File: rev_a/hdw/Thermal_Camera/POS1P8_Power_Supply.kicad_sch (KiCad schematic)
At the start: 21 parts

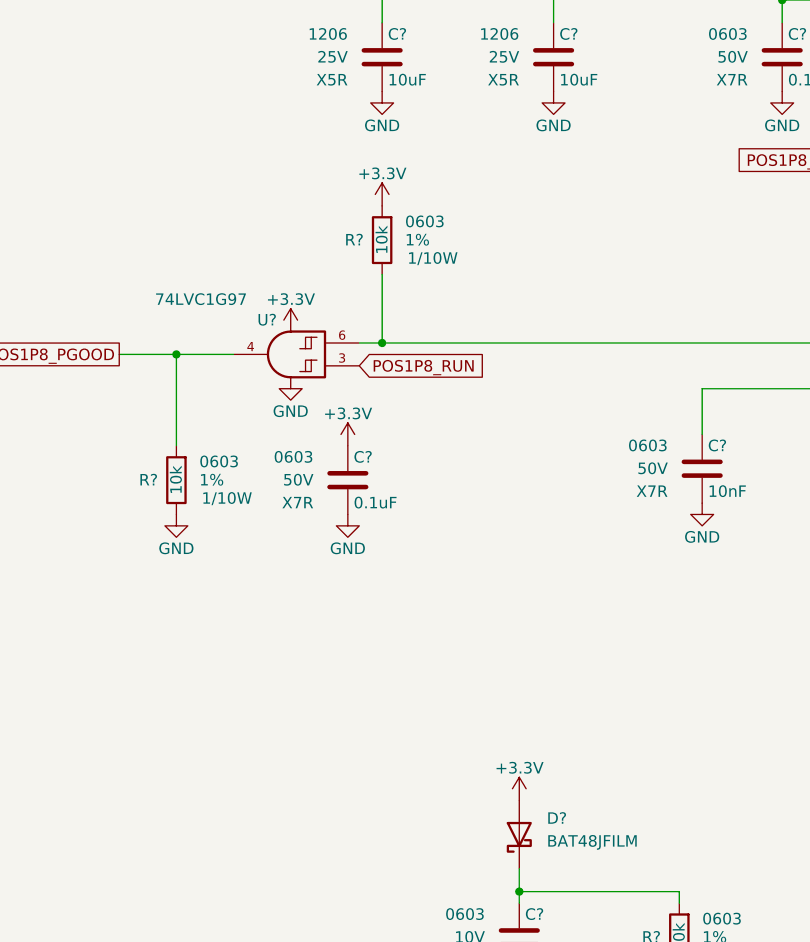
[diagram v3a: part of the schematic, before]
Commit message: changed a lot of circuits from +3.3V to +3.0V VDD
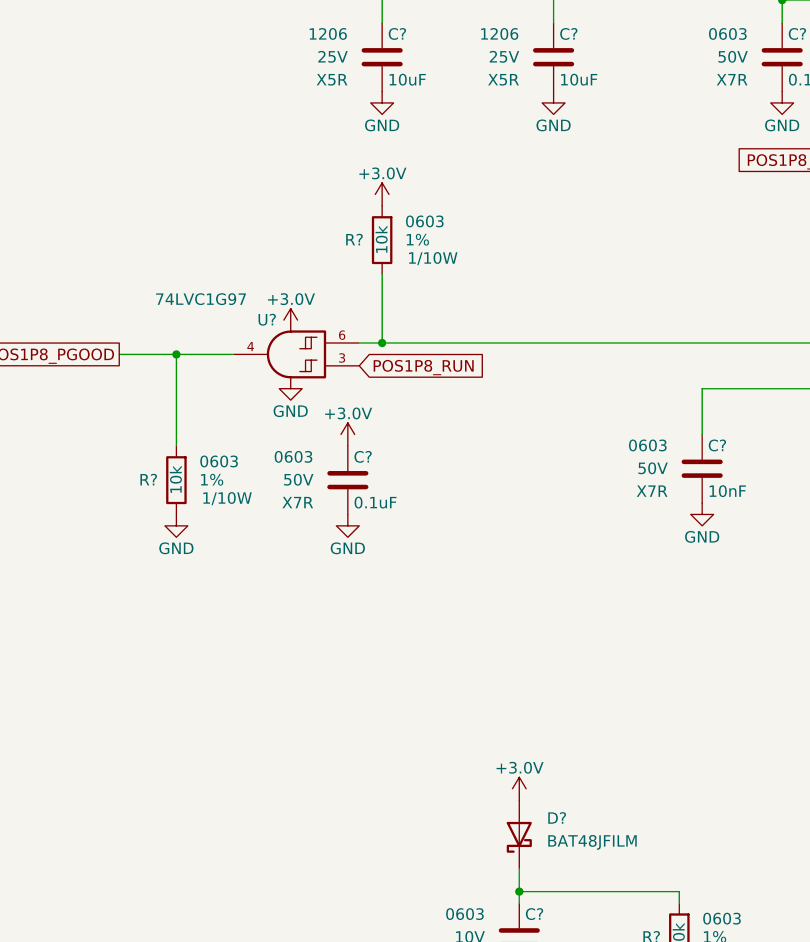
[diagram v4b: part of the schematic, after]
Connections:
- net +3.3V renamed +3.0V
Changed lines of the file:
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@@
-    )
-  )
-  (symbol (lib_id "power:+3.3V") (at 88.9 140.97 0) (unit 1)
-    (in_bom yes) (on_board yes) (dnp no)
-    (property "Reference" "#PWR0609" (at 88.9 144.78 0)
-      (effects (font (size 1.27 1.27)) hide)
-    )
-    (property "Value" "+3.3V" (at 88.9 137.414 0)
-      (effects (font (size 1.27 1.27)))
-    )
-    (property "Footprint" "" (at 88.9 140.97 0)
-      (effects (font (size 1.27 1.27)) hide)
-    )
-    (property "Datasheet" "" (at 88.9 140.97 0)
-      (effects (font (size 1.27 1.27)) hide)
-    )
-    (pin "1")
-    (instances
-      (project "Thermal_Camera"
-        (path "/4bd21e0b-5408-4b93-866e-c82ac5b31fa9/3fa2ed45-8dc3-4842-ae64-2bab78bff715"
-          (reference "#PWR0609") (unit 1)
-        )
-      )
     )
   )
@@
         (path "/e85aac8c-404c-45dd-bda3-1057cae83baf/00000000-0000-0000-0000-00005f41a7c7"
           (reference "#PWR0322") (unit 1)
-        )
-      )
-    )
-  )
-  (symbol (lib_id "power:+3.3V") (at 69.85 101.6 0) (unit 1)
-    (in_bom yes) (on_board yes) (dnp no)
-    (property "Reference" "#PWR0616" (at 69.85 105.41 0)
-      (effects (font (size 1.27 1.27)) hide)
-    )
-    (property "Value" "+3.3V" (at 69.85 98.044 0)
-      (effects (font (size 1.27 1.27)))
-    )
-    (property "Footprint" "" (at 69.85 101.6 0)
-      (effects (font (size 1.27 1.27)) hide)
-    )
-    (property "Datasheet" "" (at 69.85 101.6 0)
-      (effects (font (size 1.27 1.27)) hide)
-    )
-    (pin "1")
-    (instances
-      (project "Thermal_Camera"
-        (path "/4bd21e0b-5408-4b93-866e-c82ac5b31fa9/3fa2ed45-8dc3-4842-ae64-2bab78bff715"
-          (reference "#PWR0616") (unit 1)
         )
       )
@@
     )
   )
-  (symbol (lib_id "power:+3.3V") (at 63.5 88.9 0) (unit 1)
-    (in_bom yes) (on_board yes) (dnp no)
-    (property "Reference" "#PWR0619" (at 63.5 92.71 0)
-      (effects (font (size 1.27 1.27)) hide)
-    )
-    (property "Value" "+3.3V" (at 63.5 85.344 0)
-      (effects (font (size 1.27 1.27)))
-    )
-    (property "Footprint" "" (at 63.5 88.9 0)
-      (effects (font (size 1.27 1.27)) hide)
-    )
-    (property "Datasheet" "" (at 63.5 88.9 0)
-      (effects (font (size 1.27 1.27)) hide)
-    )
-    (pin "1")
-    (instances
-      (project "Thermal_Camera"
-        (path "/4bd21e0b-5408-4b93-866e-c82ac5b31fa9/3fa2ed45-8dc3-4842-ae64-2bab78bff715"
-          (reference "#PWR0619") (unit 1)
-        )
-      )
-    )
-  )
   (symbol (lib_id "Custom_Library:R_Custom") (at 106.68 156.21 0) (unit 1)
     (in_bom yes) (on_board yes) (dnp no)
@@
     )
   )
+  (symbol (lib_id "Custom Library:+3.0V") (at 69.85 101.6 0) (unit 1)
+    (in_bom yes) (on_board yes) (dnp no)
+    (property "Reference" "#PWR0616" (at 69.85 105.41 0)
+      (effects (font (size 1.27 1.27)) hide)
+    )
+    (property "Value" "+3.0V" (at 69.85 98.044 0)
+      (effects (font (size 1.27 1.27)))
+    )
+    (property "Footprint" "" (at 69.85 101.6 0)
+      (effects (font (size 1.27 1.27)) hide)
+    )
+    (property "Datasheet" "" (at 69.85 101.6 0)
+      (effects (font (size 1.27 1.27)) hide)
+    )
+    (pin "1")
+    (instances
+      (project "Thermal_Camera"
+        (path "/4bd21e0b-5408-4b93-866e-c82ac5b31fa9/3fa2ed45-8dc3-4842-ae64-2bab78bff715"
+          (reference "#PWR0616") (unit 1)
+        )
+      )
+    )
+  )
   (symbol (lib_id "power:GND") (at 73.66 62.23 0) (unit 1)
     (in_bom yes) (on_board yes) (dnp no)
@@
     )
   )
-  (symbol (lib_id "power:+3.3V") (at 73.66 74.93 0) (unit 1)
-    (in_bom yes) (on_board yes) (dnp no)
-    (property "Reference" "#PWR0624" (at 73.66 78.74 0)
-      (effects (font (size 1.27 1.27)) hide)
-    )
-    (property "Value" "+3.3V" (at 73.66 71.374 0)
-      (effects (font (size 1.27 1.27)))
-    )
-    (property "Footprint" "" (at 73.66 74.93 0)
-      (effects (font (size 1.27 1.27)) hide)
-    )
-    (property "Datasheet" "" (at 73.66 74.93 0)
-      (effects (font (size 1.27 1.27)) hide)
-    )
-    (pin "1")
-    (instances
-      (project "Thermal_Camera"
-        (path "/4bd21e0b-5408-4b93-866e-c82ac5b31fa9/3fa2ed45-8dc3-4842-ae64-2bab78bff715"
-          (reference "#PWR0624") (unit 1)
+  (symbol (lib_id "Custom Library:+3.0V") (at 88.9 140.97 0) (unit 1)
+    (in_bom yes) (on_board yes) (dnp no)
+    (property "Reference" "#PWR0609" (at 88.9 144.78 0)
+      (effects (font (size 1.27 1.27)) hide)
+    )
+    (property "Value" "+3.0V" (at 88.9 137.414 0)
+      (effects (font (size 1.27 1.27)))
+    )
+    (property "Footprint" "" (at 88.9 140.97 0)
+      (effects (font (size 1.27 1.27)) hide)
+    )
+    (property "Datasheet" "" (at 88.9 140.97 0)
+      (effects (font (size 1.27 1.27)) hide)
+    )
+    (pin "1")
+    (instances
+      (project "Thermal_Camera"
+        (path "/4bd21e0b-5408-4b93-866e-c82ac5b31fa9/3fa2ed45-8dc3-4842-ae64-2bab78bff715"
+          (reference "#PWR0609") (unit 1)
         )
       )
@@
     )
   )
+  (symbol (lib_id "Custom Library:+3.0V") (at 73.66 74.93 0) (unit 1)
+    (in_bom yes) (on_board yes) (dnp no)
+    (property "Reference" "#PWR0622" (at 73.66 78.74 0)
+      (effects (font (size 1.27 1.27)) hide)
+    )
+    (property "Value" "+3.0V" (at 73.66 71.374 0)
+      (effects (font (size 1.27 1.27)))
+    )
+    (property "Footprint" "" (at 73.66 74.93 0)
+      (effects (font (size 1.27 1.27)) hide)
+    )
+    (property "Datasheet" "" (at 73.66 74.93 0)
+      (effects (font (size 1.27 1.27)) hide)
+    )
+    (pin "1")
+    (instances
+      (project "Thermal_Camera"
+        (path "/4bd21e0b-5408-4b93-866e-c82ac5b31fa9/3fa2ed45-8dc3-4842-ae64-2bab78bff715"
+          (reference "#PWR0622") (unit 1)
+        )
+      )
+    )
+  )
   (symbol (lib_id "Custom_Library:R_Custom") (at 224.79 78.74 0) (unit 1)
     (in_bom yes) (on_board yes) (dnp no)
@@
         )
       )
+    )
+  )
+  (symbol (lib_id "Custom Library:+3.0V") (at 63.5 88.9 0) (unit 1)
+    (in_bom yes) (on_board yes) (dnp no)
+    (property "Reference" "#PWR0619" (at 63.5 92.71 0)
+      (effects (font (size 1.27 1.27)) hide)
+    )
+    (property "Value" "+3.0V" (at 63.5 85.344 0)
+      (effects (font (size 1.27 1.27)))
+    )
+    (property "Footprint" "" (at 63.5 88.9 0)
+      (effects (font (size 1.27 1.27)) hide)
+    )
+    (property "Datasheet" "" (at 63.5 88.9 0)
+      (effects (font (size 1.27 1.27)) hide)
+    )
+    (pin "1")
+    (instances
+      (project "Thermal_Camera"
+        (path "/4bd21e0b-5408-4b93-866e-c82ac5b31fa9/3fa2ed45-8dc3-4842-ae64-2bab78bff715"
+          (reference "#PWR0619") (unit 1)
+        )
+      )

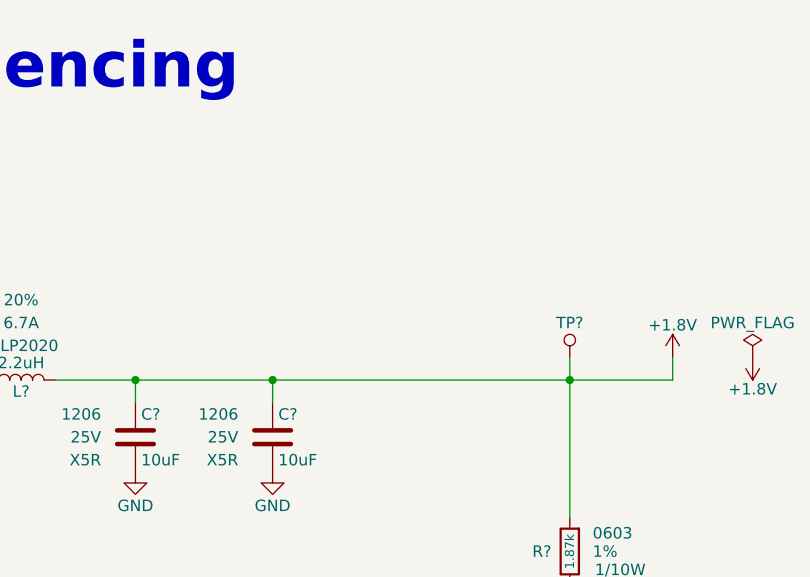
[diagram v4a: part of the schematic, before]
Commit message: added new telemetry circuits
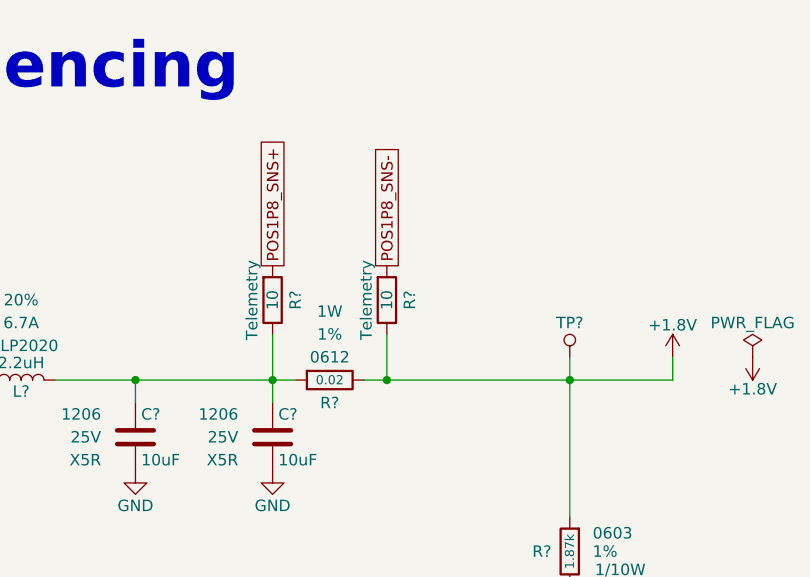
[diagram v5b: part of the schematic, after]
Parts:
- added R? (x2): 10, Resistors_SMD:R_0603, symbol Custom_Library:R_Custom
- added R?: 0.02, Resistors_SMD:R_0612, symbol Custom_Library:R_Custom
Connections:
- net +1.8V: now also R?.2, R?.2; no longer C?.1, C?.1, L?.2
- new net: C?.1, C?.1, L?.2, R?.1, R?.2
- new net POS1P8_SNS+: R?.1
- new net POS1P8_SNS-: R?.1

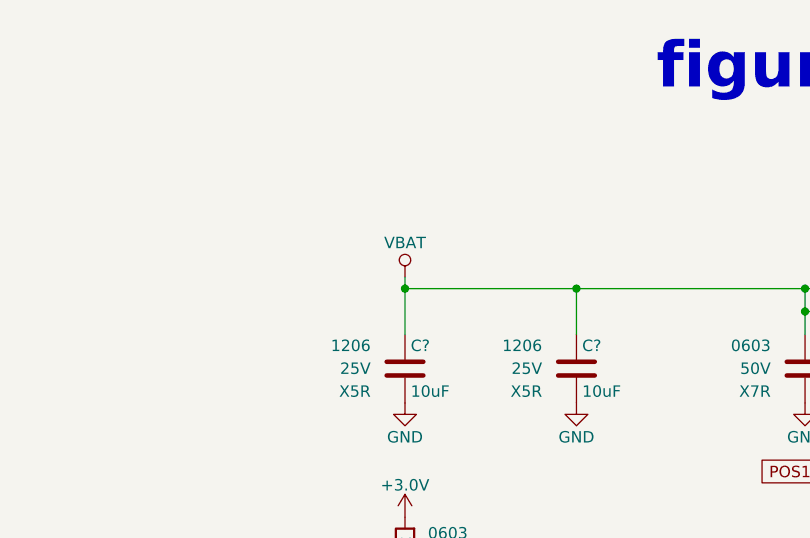
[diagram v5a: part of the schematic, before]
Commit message: added battery circuitry, LCD backlight
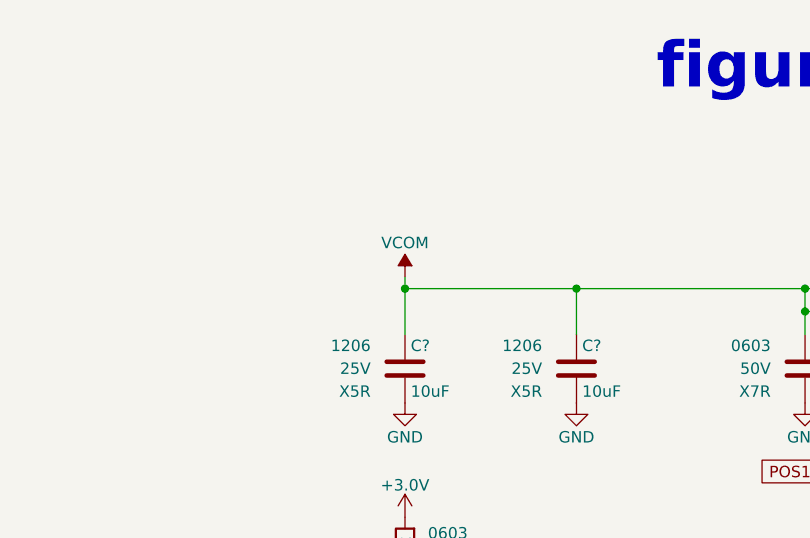
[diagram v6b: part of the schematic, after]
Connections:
- net VBAT renamed VCOM
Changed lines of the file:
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@@
-    )
-  )
-  (symbol (lib_id "Custom Library:VBAT") (at 73.66 48.26 0) (unit 1)
-    (in_bom yes) (on_board yes) (dnp no)
-    (property "Reference" "#PWR0625" (at 73.66 52.07 0)
-      (effects (font (size 1.27 1.27)) hide)
-    )
-    (property "Value" "VBAT" (at 73.66 44.45 0)
-      (effects (font (size 1.27 1.27)))
-    )
-    (property "Footprint" "" (at 73.66 48.26 0)
-      (effects (font (size 1.27 1.27)) hide)
-    )
-    (property "Datasheet" "" (at 73.66 48.26 0)
-      (effects (font (size 1.27 1.27)) hide)
-    )
-    (pin "1")
-    (instances
-      (project "Thermal_Camera"
-        (path "/4bd21e0b-5408-4b93-866e-c82ac5b31fa9/3fa2ed45-8dc3-4842-ae64-2bab78bff715"
-          (reference "#PWR0625") (unit 1)
-        )
-      )
     )
   )
@@
         )
       )
+    )
+  )
+  (symbol (lib_id "power:VCOM") (at 73.66 48.26 0) (unit 1)
+    (in_bom yes) (on_board yes) (dnp no)
+    (property "Reference" "#PWR015" (at 73.66 52.07 0)
+      (effects (font (size 1.27 1.27)) hide)
+    )
+    (property "Value" "VCOM" (at 73.66 44.45 0)
+      (effects (font (size 1.27 1.27)))
+    )
+    (property "Footprint" "" (at 73.66 48.26 0)
+      (effects (font (size 1.27 1.27)) hide)
+    )
+    (property "Datasheet" "" (at 73.66 48.26 0)
+      (effects (font (size 1.27 1.27)) hide)
+    )
+    (pin "1")
+    (instances
+      (project "Thermal_Camera"
+        (path "/4bd21e0b-5408-4b93-866e-c82ac5b31fa9/079d68a7-d67d-4f5f-9c02-dfffe75c3c82"
+          (reference "#PWR015") (unit 1)
+        )
+        (path "/4bd21e0b-5408-4b93-866e-c82ac5b31fa9/3fa2ed45-8dc3-4842-ae64-2bab78bff715"
+          (reference "#PWR016") (unit 1)
+        )
+      )

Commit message: added PIC32 bypass, SD card load switch, other random junk
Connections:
- net POS12_PGOOD renamed POS3P0_PGOOD
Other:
- note removed: "figure out sequencing"
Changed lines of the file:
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@@
     (stroke (width 0) (type default))
-  )
-  (text "figure out sequencing" (at 101.6 27.94 0)
-    (effects (font (size 5.08 5.08) (thickness 1.016) bold (color 194 0 0 1)) (justify left bottom))
   )
   (global_label "POS1P8_RUN" (shape input) (at 127 69.85 180) (fields_autoplaced)
@@
     )
   )
-  (global_label "POS12_PGOOD" (shape input) (at 41.91 168.91 180) (fields_autoplaced)
+  (global_label "POS3P0_PGOOD" (shape input) (at 41.91 168.91 180) (fields_autoplaced)
     (effects (font (size 1.27 1.27)) (justify right))
-    (property "Intersheetrefs" "${INTERSHEET_REFS}" (at 25.9908 168.91 0)
+    (property "Intersheetrefs" "${INTERSHEET_REFS}" (at 24.0666 168.91 0)
       (effects (font (size 1.27 1.27)) (justify right) hide)
     )
